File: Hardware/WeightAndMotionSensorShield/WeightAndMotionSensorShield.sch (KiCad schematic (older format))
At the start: 11 parts, among them J1 PIR, J2 CELLS, P1 Power, P2 Analog, P3 Digital, P4 Digital, P5 CONN_01X01, P6 CONN_01X01, P7 CONN_01X01, P8 CONN_01X01, U1 HX711_PCB

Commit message: Adds LED, reset button, 2nd PIR header
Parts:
- added D1: LED, LED_THT:LED_D5.0mm, symbol Device:LED
- added J3: UL, Connector_PinSocket_2.54mm:PinSocket_1x03_P2.54mm_Vertical, symbol Connector_Generic:Conn_01x03
- added J4: LL, Connector_PinHeader_2.54mm:PinHeader_1x03_P2.54mm_Vertical, symbol Connector_Generic:Conn_01x03
- added J5: CELLS, Connector_PinHeader_2.54mm:PinHeader_1x04_P2.54mm_Vertical, symbol Connector_Generic:Conn_01x04
- added J6: UR, Connector_PinHeader_2.54mm:PinHeader_1x03_P2.54mm_Vertical, symbol Connector_Generic:Conn_01x03
- added J7: LR, Connector_PinHeader_2.54mm:PinHeader_1x03_P2.54mm_Vertical, symbol Connector_Generic:Conn_01x03
- added R1: 128, Resistor_THT:R_Axial_DIN0207_L6.3mm_D2.5mm_P10.16mm_Horizontal, symbol Device:R_US
- added SW1: RESET, Button_Switch_THT:SW_PUSH_6mm, symbol Switch:SW_Push
- J1: footprint Connector_PinHeader_2.54mm:PinHeader_1x03_P2.54mm_Vertical -> Connector_PinSocket_2.54mm:PinSocket_1x03_P2.54mm_Horizontal
- J2: footprint Connector_PinHeader_2.54mm:PinHeader_1x04_P2.54mm_Vertical -> Connector_PinSocket_2.54mm:PinSocket_1x04_P2.54mm_Horizontal
- U1: symbol WeightAndMotionSensorShieldParts:HX711_PCB -> WeightAndMotionSensorShield-rescue:HX711_PCB-WeightAndMotionSensorShieldParts
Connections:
- net labels removed: 11(**/MOSI), Reset
- wire segments 29 -> 37
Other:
- moved on the sheet: J1, J2, P1, P2, P3, U1

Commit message: PCB v1.1 and 2 changes
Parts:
- added J10: CELLS, Connector_PinHeader_2.54mm:PinHeader_1x04_P2.54mm_Vertical, symbol Connector_Generic:Conn_01x04
- added J11: UR2, Connector_PinHeader_2.54mm:PinHeader_1x03_P2.54mm_Vertical, symbol Connector_Generic:Conn_01x03
- added J12: LR2, Connector_PinHeader_2.54mm:PinHeader_1x03_P2.54mm_Vertical, symbol Connector_Generic:Conn_01x03
- added J8: UL2, Connector_PinSocket_2.54mm:PinSocket_1x03_P2.54mm_Vertical, symbol Connector_Generic:Conn_01x03
- added J9: LL2, Connector_PinHeader_2.54mm:PinHeader_1x03_P2.54mm_Vertical, symbol Connector_Generic:Conn_01x03
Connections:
- new net: J11.1 (Pin_1), J12.1 (Pin_1)
- new net: J10.1 (Pin_1), J12.2 (Pin_2)
- new net: J12.3 (Pin_3), J9.3 (Pin_3)
- new net: J8.1 (Pin_1), J9.1 (Pin_1)
- new net: J10.4 (Pin_4), J9.2 (Pin_2)
- new net: J10.3 (Pin_3), J11.2 (Pin_2)
- new net: J11.3 (Pin_3), J8.3 (Pin_3)
- new net: J10.2 (Pin_2), J8.2 (Pin_2)
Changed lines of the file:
@@
 Wire Wire Line
 	4300 3800 5100 3800
+$Comp
+L Connector_Generic:Conn_01x03 J12
+U 1 1 5D3800F0
+P 10250 6100
+F 0 "J12" H 10400 6100 50  0000 R CNN
+F 1 "LR2" H 10450 6200 50  0000 R CNN
+F 2 "Connector_PinHeader_2.54mm:PinHeader_1x03_P2.54mm_Vertical" H 10250 6100 50  0001 C CNN
+F 3 "~" H 10250 6100 50  0001 C CNN
+	1    10250 6100
+	1    0    0    1
+$EndComp
+$Comp
+L Connector_Generic:Conn_01x03 J9
+U 1 1 5D3800F7
+P 9350 6100
+F 0 "J9" H 9500 6100 50  0000 R CNN
+F 1 "LL2" H 9550 6200 50  0000 R CNN
+F 2 "Connector_PinHeader_2.54mm:PinHeader_1x03_P2.54mm_Vertical" H 9350 6100 50  0001 C CNN
+F 3 "~" H 9350 6100 50  0001 C CNN
+	1    9350 6100
+	-1   0    0    1
+$EndComp
+$Comp
+L Connector_Generic:Conn_01x03 J11
+U 1 1 5D3800FE
+P 10250 5400
+F 0 "J11" H 10400 5400 50  0000 R CNN
+F 1 "UR2" H 10450 5500 50  0000 R CNN
+F 2 "Connector_PinHeader_2.54mm:PinHeader_1x03_P2.54mm_Vertical" H 10250 5400 50  0001 C CNN
+F 3 "~" H 10250 5400 50  0001 C CNN
+	1    10250 5400
+	1    0    0    1
+$EndComp
+$Comp
+L Connector_Generic:Conn_01x03 J8
+U 1 1 5D380105
+P 9350 5400
+F 0 "J8" H 9500 5400 50  0000 R CNN
+F 1 "UL2" H 9550 5500 50  0000 R CNN
+F 2 "Connector_PinSocket_2.54mm:PinSocket_1x03_P2.54mm_Vertical" H 9350 5400 50  0001 C CNN
+F 3 "~" H 9350 5400 50  0001 C CNN
+	1    9350 5400
+	-1   0    0    1
+$EndComp
+$Comp
+L Connector_Generic:Conn_01x04 J10
+U 1 1 5D38010C
+P 9750 4850
+F 0 "J10" H 9829 4842 50  0000 L CNN
+F 1 "CELLS" H 9829 4751 50  0000 L CNN
+F 2 "Connector_PinHeader_2.54mm:PinHeader_1x04_P2.54mm_Vertical" H 9750 4850 50  0001 C CNN
+F 3 "~" H 9750 4850 50  0001 C CNN
+	1    9750 4850
+	0    -1   -1   0
+$EndComp
+Wire Wire Line
+	9750 5400 9750 5050
+Wire Wire Line
+	9850 5400 9850 5050
+Wire Wire Line
+	9550 5400 9750 5400
+Wire Wire Line
+	9850 5400 10050 5400
+Wire Wire Line
+	9950 5700 9950 5050
+Wire Wire Line
+	9800 5650 9650 5650
+Wire Wire Line
+	9650 5650 9650 5050
+Wire Wire Line
+	9550 6100 9650 6100
+Wire Wire Line
+	9650 5700 9650 6100
+Wire Wire Line
+	9650 5700 9950 5700
+Wire Wire Line
+	9950 6100 10050 6100
+Wire Wire Line
+	9800 5650 9800 5750
+Wire Wire Line
+	9800 5750 9950 5750
+Wire Wire Line
+	9950 5750 9950 6100
+Wire Wire Line
+	9550 5300 10050 5300
+Wire Wire Line
+	9550 5500 9600 5500
+Wire Wire Line
+	9600 5500 9600 6200
+Wire Wire Line
+	9600 6200 9550 6200
+Wire Wire Line
+	10050 6200 10000 6200
+Wire Wire Line
+	10000 6200 10000 5500
+Wire Wire Line
+	10000 5500 10050 5500
+Wire Wire Line
+	9550 6000 10050 6000
 $EndSCHEMATC

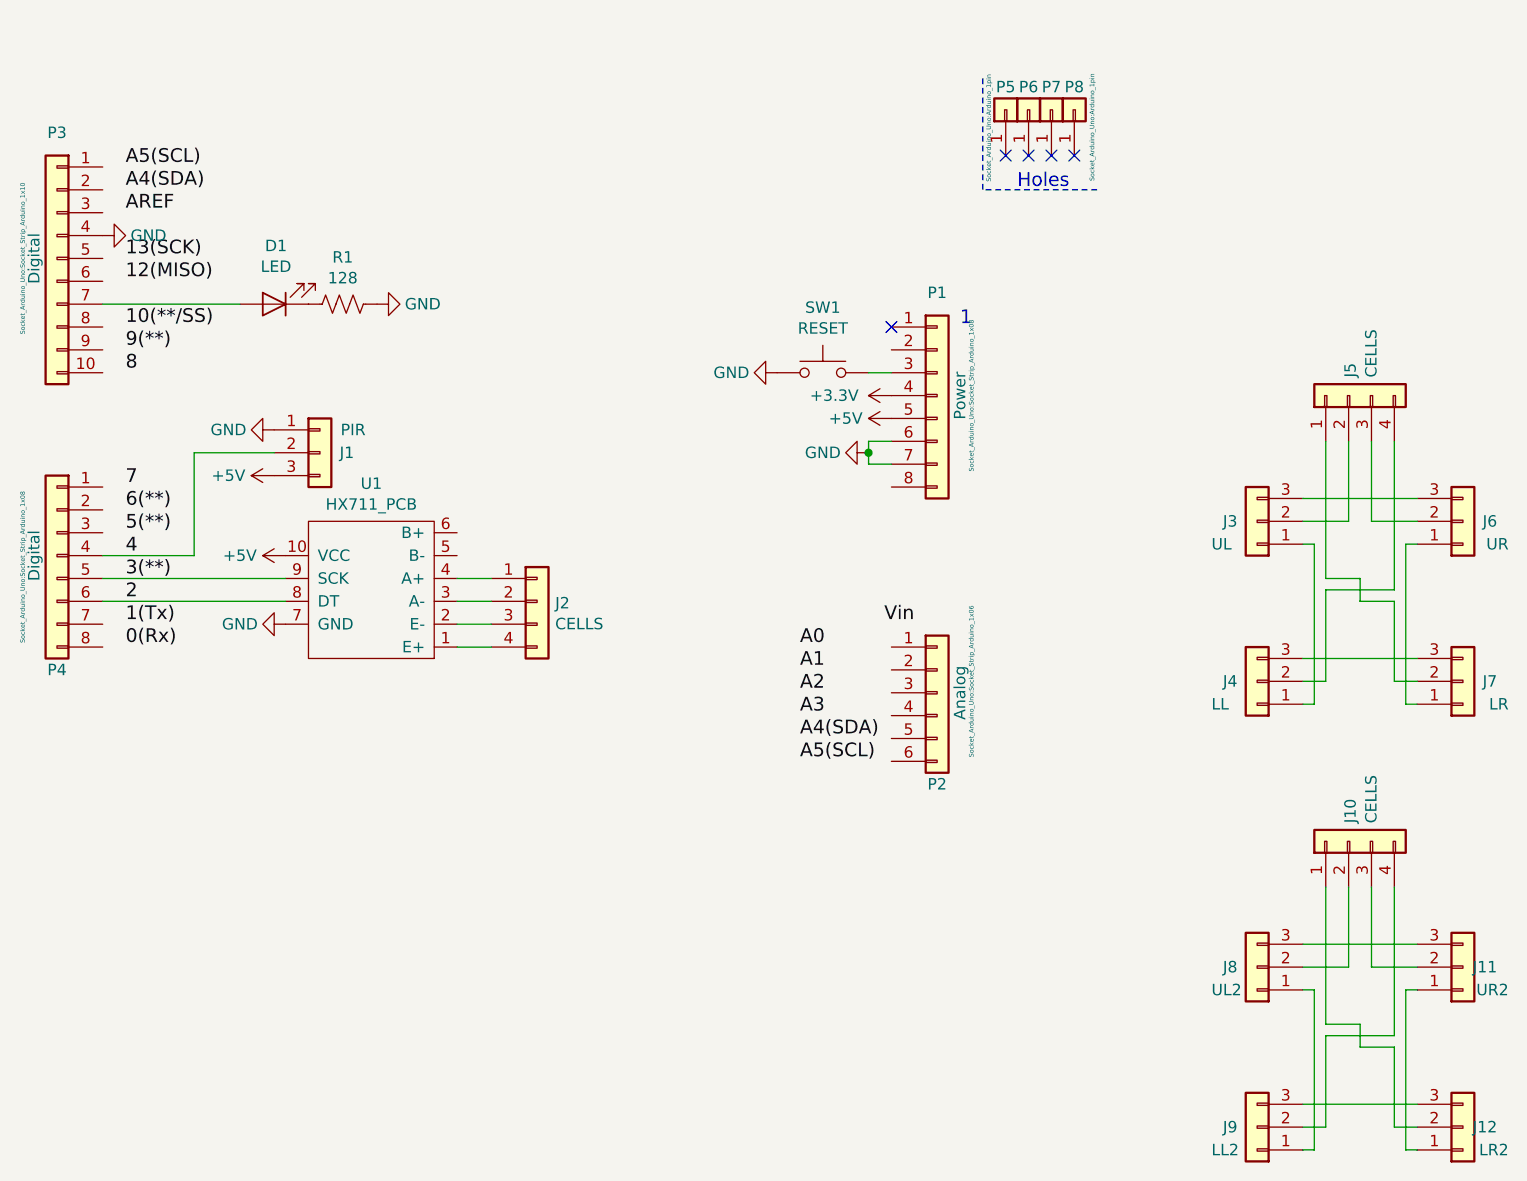
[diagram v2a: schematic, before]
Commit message: Add header for HC-05 module
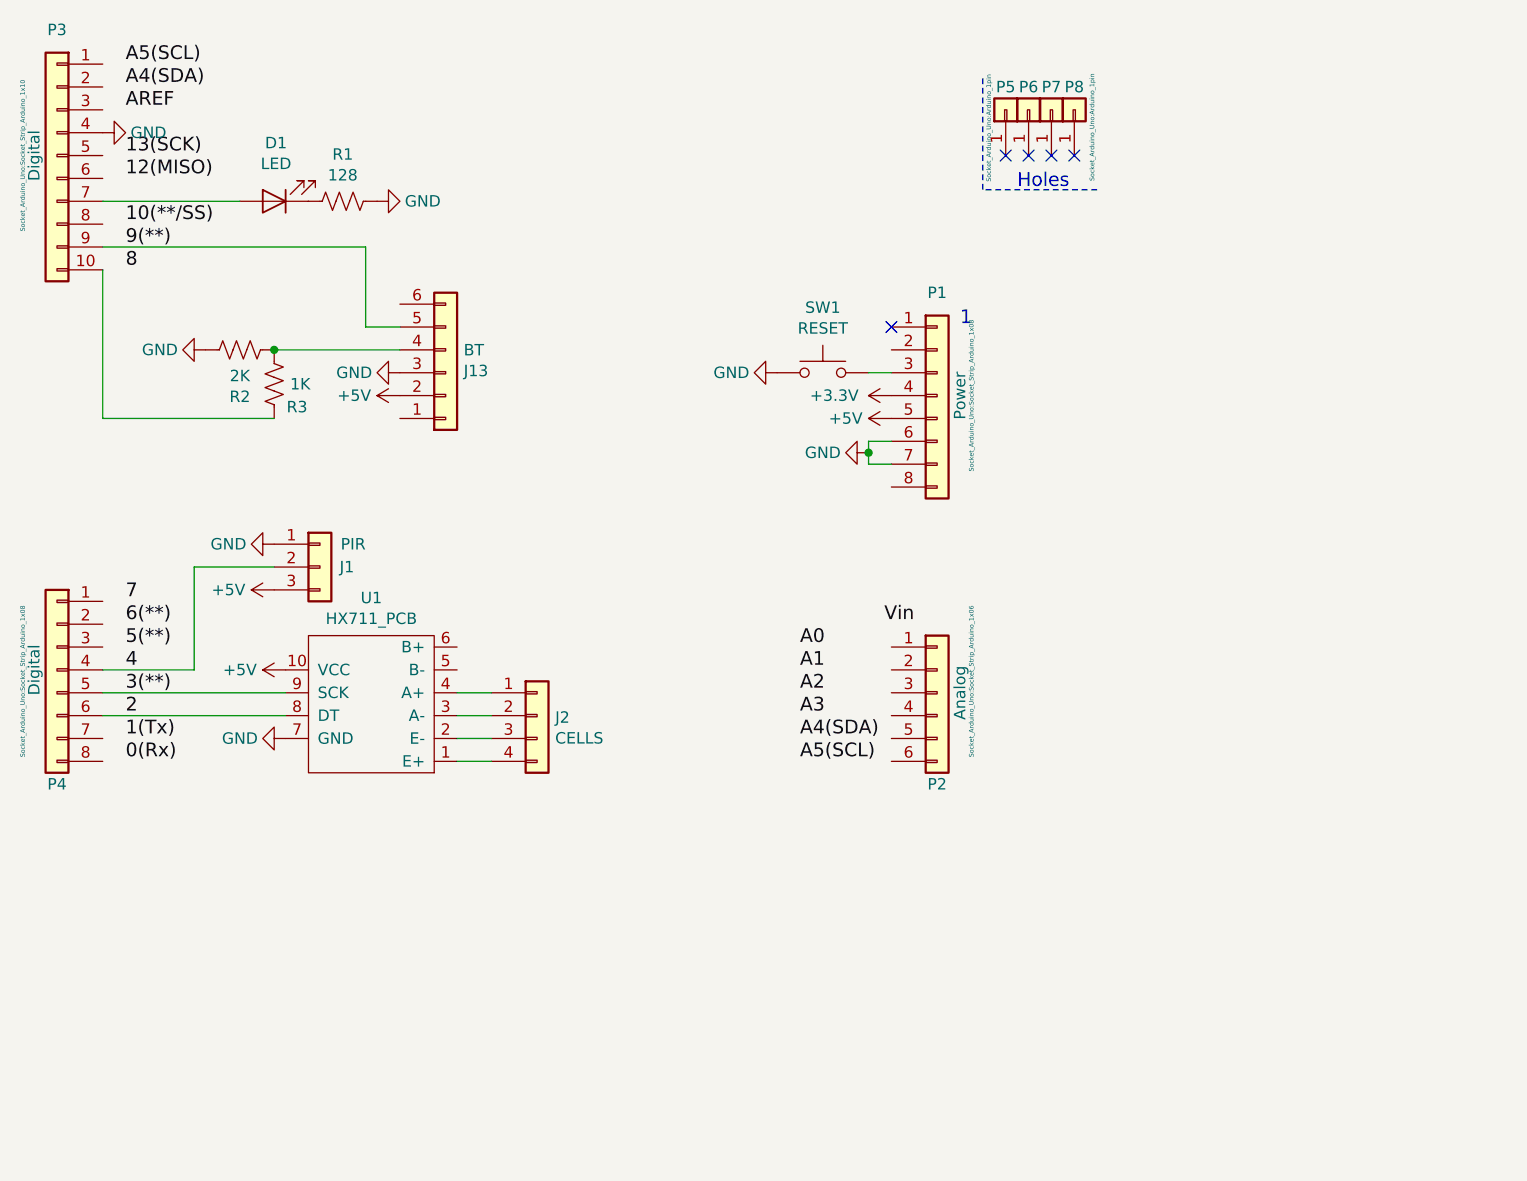
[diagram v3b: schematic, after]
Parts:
- removed J10, J5: CELLS, Connector_PinHeader_2.54mm:PinHeader_1x04_P2.54mm_Vertical, symbol Connector_Generic:Conn_01x04
- removed J11: UR2, Connector_PinHeader_2.54mm:PinHeader_1x03_P2.54mm_Vertical, symbol Connector_Generic:Conn_01x03
- removed J12: LR2, Connector_PinHeader_2.54mm:PinHeader_1x03_P2.54mm_Vertical, symbol Connector_Generic:Conn_01x03
- removed J3: UL, Connector_PinSocket_2.54mm:PinSocket_1x03_P2.54mm_Vertical, symbol Connector_Generic:Conn_01x03
- removed J4: LL, Connector_PinHeader_2.54mm:PinHeader_1x03_P2.54mm_Vertical, symbol Connector_Generic:Conn_01x03
- removed J6: UR, Connector_PinHeader_2.54mm:PinHeader_1x03_P2.54mm_Vertical, symbol Connector_Generic:Conn_01x03
- removed J7: LR, Connector_PinHeader_2.54mm:PinHeader_1x03_P2.54mm_Vertical, symbol Connector_Generic:Conn_01x03
- removed J8: UL2, Connector_PinSocket_2.54mm:PinSocket_1x03_P2.54mm_Vertical, symbol Connector_Generic:Conn_01x03
- removed J9: LL2, Connector_PinHeader_2.54mm:PinHeader_1x03_P2.54mm_Vertical, symbol Connector_Generic:Conn_01x03
- added J13: BT, Connector_PinHeader_2.54mm:PinHeader_1x06_P2.54mm_Vertical, symbol Connector_Generic:Conn_01x06
- added R2: 2K, Resistor_THT:R_Axial_DIN0207_L6.3mm_D2.5mm_P10.16mm_Horizontal, symbol Device:R_US
- added R3: 1K, Resistor_THT:R_Axial_DIN0207_L6.3mm_D2.5mm_P10.16mm_Horizontal, symbol Device:R_US
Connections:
- net +5V: now also J13.2 (Pin_2)
- net 9(**): now also P3.9 (Pin_9), J13.5 (Pin_5)
- net GND: now also J13.3 (Pin_3), R2.1
- net at P3.10 (Pin_10): now also R3.1
- new net: J13.4 (Pin_4), R2.2, R3.2
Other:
- moved on the sheet: D1, J1, J2, P3, P4, R1, U1
